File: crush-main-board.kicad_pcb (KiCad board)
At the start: 4 copper layers, 38 parts, among them J1 4x4_Header, J10 3x3 Header, J11 3x3 Header, J12 3x2 Header, J13 3x4_Header, J14 3x4_Header, J15 2157601008, J2 4x4_Header, J3 6x2_Header, J4 3x1_Header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

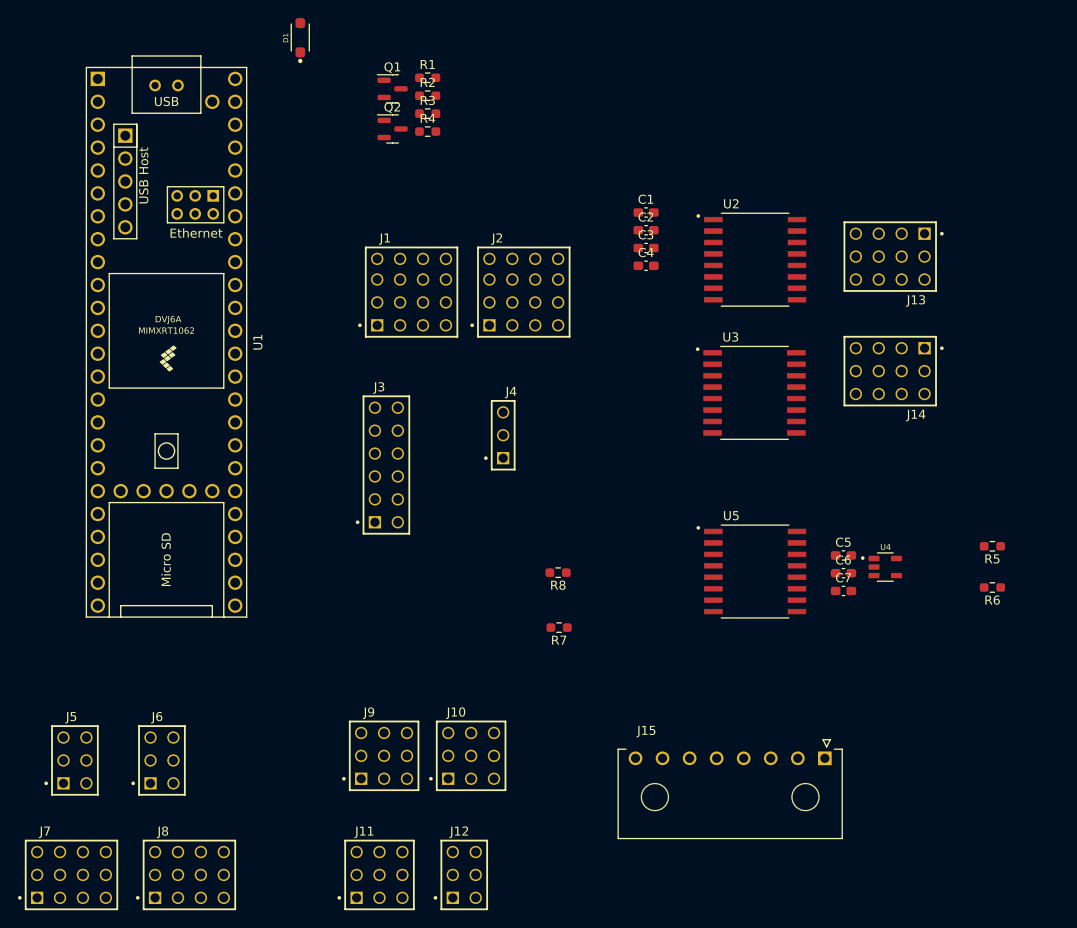
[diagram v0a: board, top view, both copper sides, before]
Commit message: Fixed some minor errors and arranged the components into two ground sides
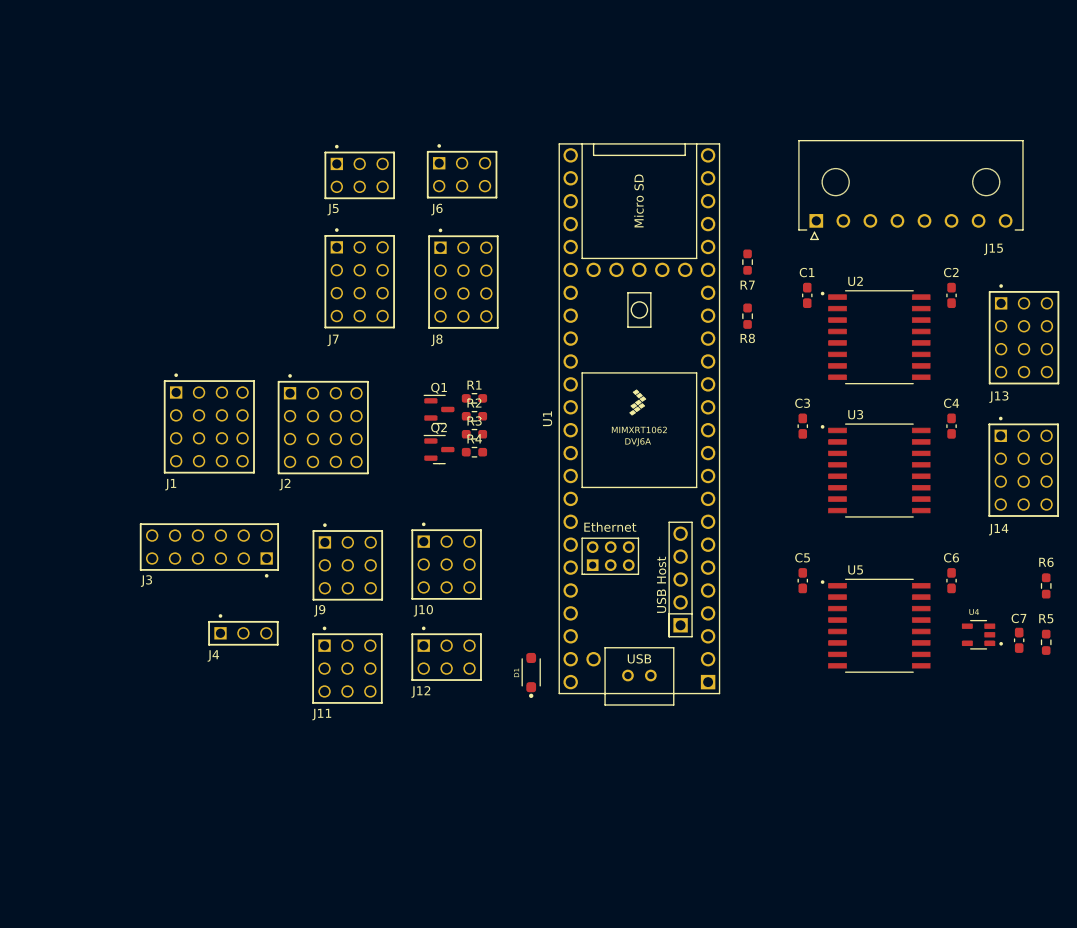
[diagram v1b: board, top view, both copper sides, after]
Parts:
- moved D1 74.9 mm to (147.4, 97.4)
- moved J7 73.2 mm to (128.4, 54.1), turned to -90 degrees
- moved J6 73.0 mm to (139.7, 42.2), turned to -90 degrees
- moved J8 72.4 mm to (139.9, 54.1), turned to -90 degrees
- moved J5 72.2 mm to (128.4, 42.3), turned to -90 degrees
- moved J15 59.6 mm to (179.0, 47.3), turned to 180 degrees
- moved U1 53.1 mm to (159.4, 69.3), turned to 90 degrees
- moved R7 45.6 mm to (171.4, 51.9), turned to -90 degrees
- moved C4 38.3 mm to (194.0, 70.1), turned to 90 degrees
- moved J4 36.2 mm to (115.5, 93.1), turned to -90 degrees
- moved Q1 35.9 mm to (137.2, 68.3)
- moved R1 35.9 mm to (141.1, 67.0)
- moved R3 35.9 mm to (141.1, 71.0)
- moved R4 35.9 mm to (141.1, 73.0)
- moved Q2 35.9 mm to (137.2, 72.7)
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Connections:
- C6 pad 2: +3V3 -> +3V3_T
- C7 pad 2: +3V3 -> +3V3_T
- U3 pad 3: PWM2 -> PWM6
- U3 pad 4: PWM3 -> PWM7
- U3 pad 5: PWM4 -> PWM8
- U3 pad 6: PWM5 -> PWM9
- U4 pad 1: +3V3 -> +3V3_T
- U5 pad 14: +3V3 -> +3V3_T

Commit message: arranged all components to be ready for routing
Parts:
- moved R5 42.7 mm to (184.4, 56.4)
- moved R6 42.7 mm to (184.4, 50.1)
- moved C5 42.7 mm to (157.4, 49.5)
- moved C6 42.7 mm to (173.9, 49.5)
- moved C7 42.7 mm to (181.4, 56.2)
- moved U4 42.7 mm to (176.9, 55.5)
- moved U5 42.7 mm to (165.9, 54.5)
- moved R1 27.8 mm to (114.1, 60.2), turned to -90 degrees
- moved R2 24.6 mm to (118.1, 60.2), turned to -90 degrees
- moved C1 23.0 mm to (157.9, 66.6)
- moved C2 23.0 mm to (173.9, 66.6)
- moved C3 23.0 mm to (157.4, 81.1)
- moved C4 23.0 mm to (173.9, 81.1)
- moved J14 23.0 mm to (181.9, 86.0)
- moved U2 23.0 mm to (165.9, 71.3)
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
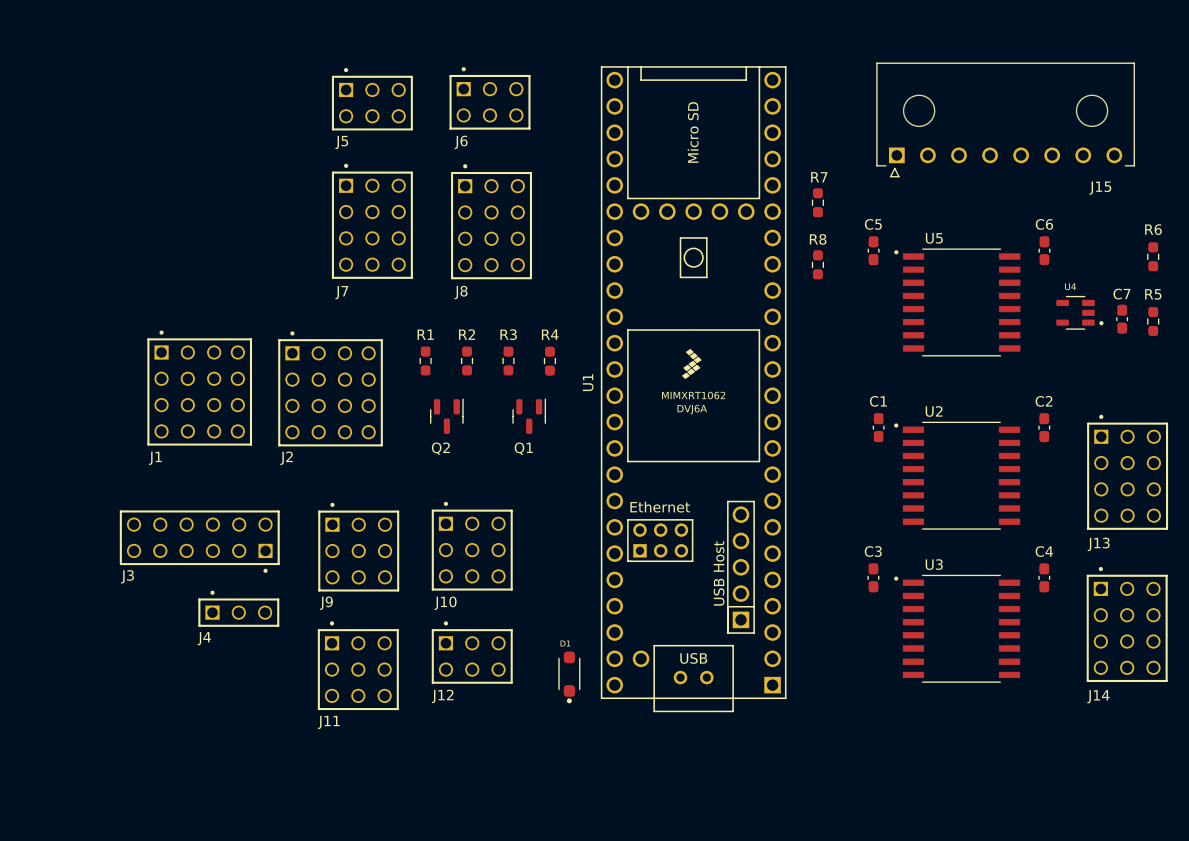
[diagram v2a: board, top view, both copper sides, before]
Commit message: re-aligned the elements based on their grounds
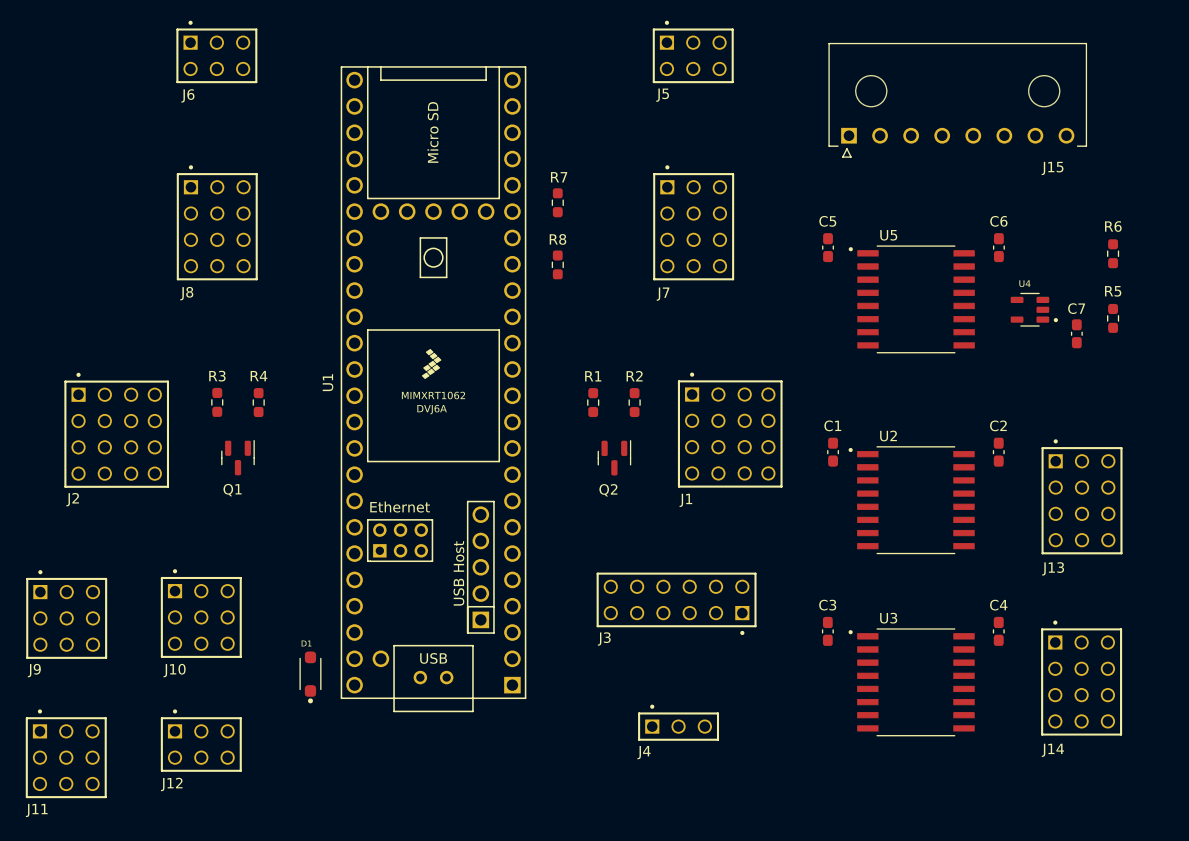
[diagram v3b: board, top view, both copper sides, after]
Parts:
- moved J1 51.4 mm to (143.7, 67.2)
- moved J3 46.4 mm to (138.3, 83.3)
- moved J4 43.9 mm to (138.5, 95.5)
- moved J5 31.3 mm to (140.0, 30.7)
- moved J7 31.0 mm to (140.0, 47.2)
- moved J11 29.5 mm to (79.4, 98.5)
- moved J9 28.9 mm to (79.5, 85.1)
- moved Q1 28.4 mm to (96.0, 69.6)
- moved R3 28.4 mm to (94.0, 64.2)
- moved R4 28.4 mm to (98.0, 64.2)
- moved J12 27.5 mm to (92.5, 97.2)
- moved J10 27.0 mm to (92.5, 85.0)
- moved J6 26.8 mm to (94.0, 30.7)
- moved J8 26.5 mm to (94.0, 47.2)
- moved R7 25.1 mm to (126.9, 44.9)
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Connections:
- J1 pad 01: +5V -> +3V3
- J1 pad 05: +5V -> +3V3
- J1 pad 09: +5V -> +3V3
- J1 pad 13: +5V -> +3V3
- J8 pad 02: +3V3 -> +5V
- J8 pad 05: +3V3 -> +5V
- J8 pad 08: +3V3 -> +5V
- J8 pad 11: +3V3 -> +5V

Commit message: Start laying out main board
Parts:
- added C7: 0u1, Capacitor_SMD:C_0603_1608Metric_Pad1.08x0.95mm_HandSolder, F.Cu at (131.4, 55.9)
- added INA232B1: ~, Package_TO_SOT_SMD:SOT-23-8_Handsoldering, F.Cu at (133.4, 49.2)
- added J16: Conn_01x02_Pin, Connector_JST:JST_XH_S2B-XH-A_1x02_P2.50mm_Horizontal, F.Cu at (77.4, 98.7)
- added J18: Conn_01x02_Pin, Connector_JST:JST_XH_S2B-XH-A_1x02_P2.50mm_Horizontal, F.Cu at (86.8, 98.7)
- added Q3: BSN20, Package_TO_SOT_SMD:SOT-23, F.Cu at (61.9, 100.7)
- added Q5: DMG2301L, Package_TO_SOT_SMD:SOT-23, F.Cu at (67.0, 108.3)
- added R5: 2k4, Resistor_SMD:R_0603_1608Metric_Pad0.98x0.95mm_HandSolder, F.Cu at (67.0, 101.6)
- added R7: 2k4, Resistor_SMD:R_0603_1608Metric_Pad0.98x0.95mm_HandSolder, F.Cu at (61.9, 104.1)
- R1, R2, R3, R4: value 4K7 -> 2k4
- moved R4 71.9 mm to (44.6, 112.3), turned to 0 degrees
- moved R3 67.3 mm to (44.6, 109.8), turned to 0 degrees
- moved Q1 63.0 mm to (44.8, 106.4), turned to 0 degrees
- moved C1 59.4 mm to (94.9, 58.9)
- moved C2 59.4 mm to (110.9, 58.9)
- moved C3 59.4 mm to (94.4, 76.2)
- moved C4 59.4 mm to (110.9, 76.2)
- moved J14 59.4 mm to (118.9, 81.1)
- moved R1 59.4 mm to (71.7, 54.1)
- moved R2 59.4 mm to (75.7, 54.1)
- moved U2 59.4 mm to (102.9, 63.5)
- moved U3 59.4 mm to (102.9, 81.1)
- moved D1 59.4 mm to (44.4, 80.3)
- moved J11 59.4 mm to (20.9, 88.4)
- moved J12 59.4 mm to (33.9, 87.1)
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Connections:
- Q1 pad 1: +5V -> +3V3

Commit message: Add changes to pcb
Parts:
- removed the C7 at (118.4, 47.5)
- removed the C7 at (131.4, 55.9)
- removed J18: Conn_01x02_Pin, Connector_JST:JST_XH_S2B-XH-A_1x02_P2.50mm_Horizontal
- removed the R5 at (121.9, 46.0)
- removed the R5 at (67.0, 101.6)
- removed R6, R8: 10K, Resistor_SMD:R_0603_1608Metric_Pad0.98x0.95mm_HandSolder
- removed the R7 at (68.3, 34.8)
- removed the R7 at (61.9, 104.1)
- removed U5: ISO1640DBR, Crush_Mainboard_Footprints:SOIC127P1030X265-16N
- added C7: 0u1, Capacitor_SMD:C_0603_1608Metric_Pad1.08x0.95mm_HandSolder, F.Cu at (113.9, 30.5)
- added C8: 0u1, Capacitor_SMD:C_0603_1608Metric_Pad1.08x0.95mm_HandSolder, F.Cu at (44.2, 40.5)
- added INA232B2: ~, Package_TO_SOT_SMD:SOT-23-8_Handsoldering, F.Cu at (44.5, 35.9)
- added J17: Conn_01x02, Connector_PinHeader_2.54mm:PinHeader_1x02_P2.54mm_Vertical, F.Cu at (30.5, 94.0)
- added R5: 2k4, Resistor_SMD:R_0603_1608Metric_Pad0.98x0.95mm_HandSolder, F.Cu at (26.5, 85.4)
- added R7: 2k4, Resistor_SMD:R_0603_1608Metric_Pad0.98x0.95mm_HandSolder, F.Cu at (26.5, 87.9)
- J1: footprint Crush_Mainboard_Footprints:4x4_Header -> Crush_Mainboard_Footprints:3x1_Header
- J16: value Conn_01x02_Pin -> Conn_01x02; footprint Connector_JST:JST_XH_S2B-XH-A_1x02_P2.50mm_Horizontal -> Connector_PinHeader_2.54mm:PinHeader_1x02_P2.54mm_Vertical
- U4: value MCP3221A5T-I/OT -> ISO1640DBR; footprint Crush_Mainboard_Footprints:SOT95P280X145-5N -> Crush_Mainboard_Footprints:SOIC127P1030X265-16N
- moved C5 83.9 mm to (53.3, 33.0), turned to 0 degrees
- moved J1 68.7 mm to (17.8, 71.1), turned to 0 degrees
- moved U1 68.4 mm to (-10.7, 66.1), turned to -90 degrees
- moved J2 60.6 mm to (74.9, 92.7), turned to 0 degrees
- moved J12 58.6 mm to (19.1, 30.5), turned to 0 degrees
- moved J5 55.6 mm to (26.7, 30.5), turned to 0 degrees
- moved D1 54.7 mm to (-5.97, 101.6), turned to 0 degrees
- moved J7 53.2 mm to (28.6, 42.9), turned to 0 degrees
- moved J3 50.7 mm to (29.2, 69.8), turned to 0 degrees
- moved J16 49.2 mm to (30.5, 83.8)
- moved J15 48.5 mm to (47.9, 26.8)
- moved Q5 48.3 mm to (21.9, 90.8)
- moved R2 46.3 mm to (44.1, 87.9), turned to 0 degrees
- moved J4 45.2 mm to (35.6, 94.0), turned to 0 degrees
- moved U4 42.7 mm to (89.3, 40.6), turned to 0 degrees
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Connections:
- INA232B1 pad 1: BATT_T -> BATT
- INA232B1 pad 2: BATT_T -> BATT
- INA232B1 pad 5: /Thruster Battery Monitoring/SCL_T -> /SCL_T
- INA232B1 pad 6: /Thruster Battery Monitoring/SDA_T -> /SDA_T
- J15 pad 6: BATT_T -> BATT
- J16 pad 1: Kill -> HW_KILL_2
- J16 pad 2: A/DIO26 -> HW_KILL_1
- Q3 pad 2: A/DIO26 -> HW_KILL_2
- U1 pad 18: A/DIO26 -> HW_KILL_2
- U1 pad 19: Kill -> HW_KILL_1
- U4 pad 1: +3V3_T -> (no net)
- U4 pad 2: GND_T -> (no net)
- U4 pad 3: /Thruster Battery Monitoring/V_REF (3V3) -> +3V3
- U4 pad 4: /Thruster Battery Monitoring/SDA_T -> (no net)
- U4 pad 5: /Thruster Battery Monitoring/SCL_T -> SDA_3V3
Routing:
- added copper zone on B.Cu, net GND
- added copper zone on B.Cu, net GND_T
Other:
- copper layers 4 -> 2

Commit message: Fixed import issues from sch to pcb
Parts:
- J1: footprint Crush_Mainboard_Footprints:3x1_Header -> Crush_Mainboard_Footprints:4x4_Header
- U4: value ISO1640DBR -> ISO1640BDR; footprint Crush_Mainboard_Footprints:SOIC127P1030X265-16N -> Package_SO:SOIC-8_3.9x4.9mm_P1.27mm
- U5: renamed from INA232B2; value ~ -> INA232B
- U6: renamed from INA232B1; value ~ -> INA232B
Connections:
- U4 pad 1: (no net) -> +3V3
- U4 pad 2: (no net) -> SDA_3V3
- U4 pad 3: +3V3 -> SCL_3V3
- U4 pad 4: (no net) -> GND_T
- U4 pad 5: SDA_3V3 -> GND_T
- U4 pad 6: SCL_3V3 -> /SCL_T
- U4 pad 7: GND_T -> /SDA_T
- U4 pad 8: (no net) -> +3V3_T

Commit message: basic routing
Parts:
- added H1: MountingHole_Pad, MountingHole:MountingHole_4.3mm_M4_Pad_Via, F.Cu at (1.52, 9.87)
- added H2: MountingHole_Pad, MountingHole:MountingHole_4.3mm_M4_Pad_Via, F.Cu at (1.52, 20.0)
- added H3: MountingHole_Pad, MountingHole:MountingHole_4.3mm_M4_Pad_Via, F.Cu at (1.52, 30.2)
- added H4: MountingHole_Pad, MountingHole:MountingHole_4.3mm_M4_Pad_Via, F.Cu at (1.52, 40.3)
- moved D1 94.4 mm to (52.0, 27.1), turned to 180 degrees
- moved J1 82.5 mm to (83.2, 20.9)
- moved J15 75.0 mm to (24.8, 98.2), turned to -90 degrees
- moved J2 72.0 mm to (69.4, 20.9)
- moved R3 70.7 mm to (80.8, 30.0), turned to 180 degrees
- moved R4 68.2 mm to (69.5, 29.6)
- moved J12 66.4 mm to (31.6, 95.6), turned to 180 degrees
- moved Q2 65.9 mm to (77.0, 31.3), turned to 90 degrees
- moved J4 60.1 mm to (36.5, 33.8), turned to 180 degrees
- moved Q1 60.1 mm to (73.2, 31.5), turned to 90 degrees
- moved R1 60.1 mm to (77.7, 35.5), turned to 90 degrees
- moved R2 59.7 mm to (73.5, 36.0), turned to 90 degrees
- moved U1 59.0 mm to (47.7, 57.9)
- moved J9 43.3 mm to (56.5, 96.2), turned to 180 degrees
- moved R7 37.8 mm to (24.8, 50.1), turned to 180 degrees
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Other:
- board outline added: 101.6 x 120.6 mm
